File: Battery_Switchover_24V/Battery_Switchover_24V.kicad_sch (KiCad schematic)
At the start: 0 parts

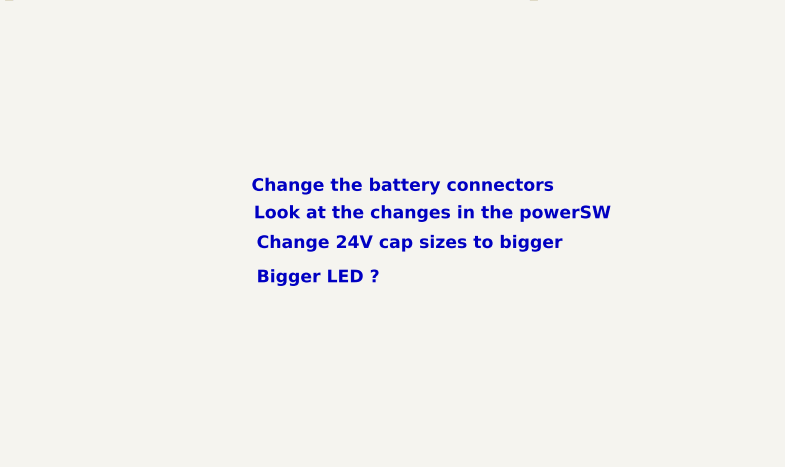
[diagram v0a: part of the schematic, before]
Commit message: Minor placement changes
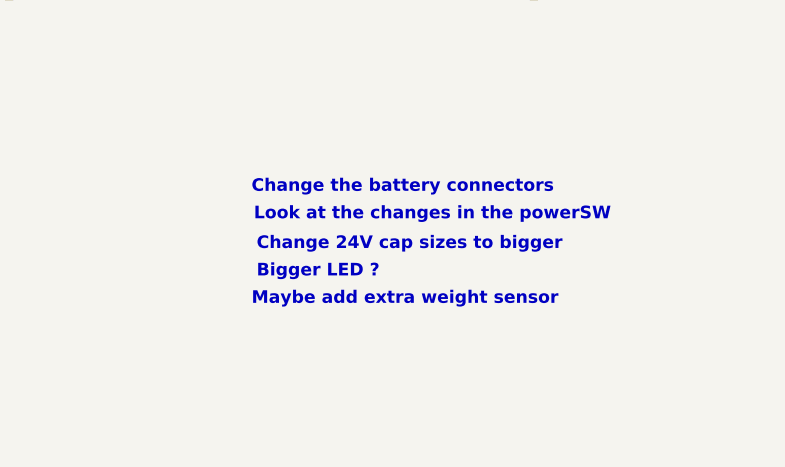
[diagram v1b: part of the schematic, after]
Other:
- note added: "Maybe add extra weight sensor"
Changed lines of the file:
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@@
+		)
+	)
+	(text "Maybe add extra weight sensor"
+		(exclude_from_sim no)
+		(at 201.168 109.22 0)
+		(effects
+			(font
+				(size 1.397 1.397)
+				(thickness 0.2794)
+				(bold yes)
+			)
 		)
 	)
@@
 	(text "Bigger LED ?"
 		(exclude_from_sim no)
-		(at 191.516 106.934 0)
+		(at 191.516 106.172 0)
 		(effects
 			(font

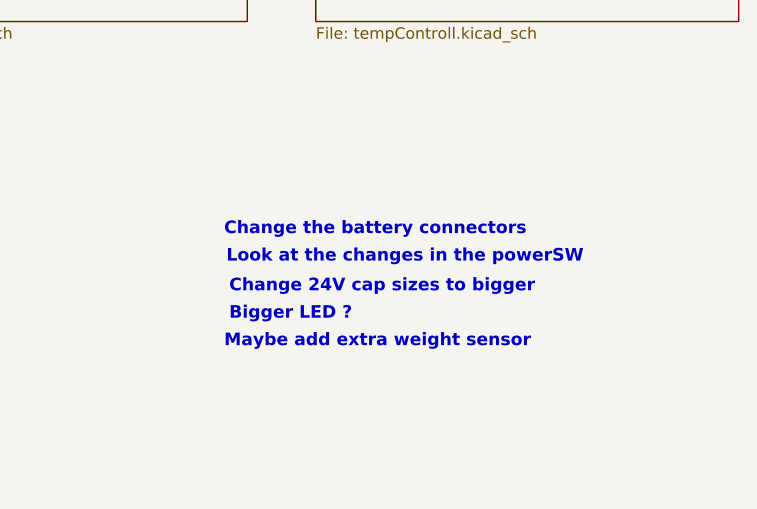
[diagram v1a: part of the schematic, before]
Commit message: Added 6 Pin ATX Connector
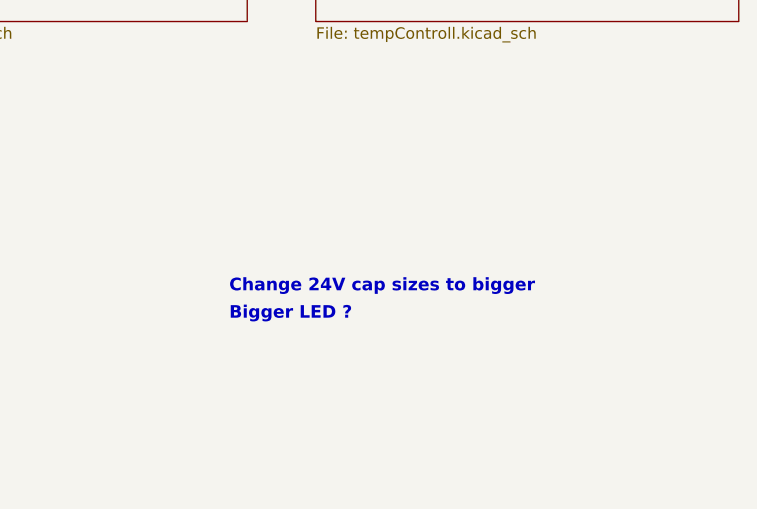
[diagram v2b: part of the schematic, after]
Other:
- note removed: "Change the battery connectors"
- note removed: "Look at the changes in the powerSW"
- note removed: "Maybe add extra weight sensor"
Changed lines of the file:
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@@
-		)
-	)
-	(text "Change the battery connectors"
-		(exclude_from_sim no)
-		(at 200.914 96.774 0)
-		(effects
-			(font
-				(size 1.397 1.397)
-				(thickness 0.2794)
-				(bold yes)
-			)
-		)
-	)
-	(text "Maybe add extra weight sensor"
-		(exclude_from_sim no)
-		(at 201.168 109.22 0)
-		(effects
-			(font
-				(size 1.397 1.397)
-				(thickness 0.2794)
-				(bold yes)
-			)
-		)
-	)
-	(text "Look at the changes in the powerSW"
-		(exclude_from_sim no)
-		(at 204.216 99.822 0)
-		(effects
-			(font
-				(size 1.397 1.397)
-				(thickness 0.254)
-				(bold yes)
-			)
 		)
 	)

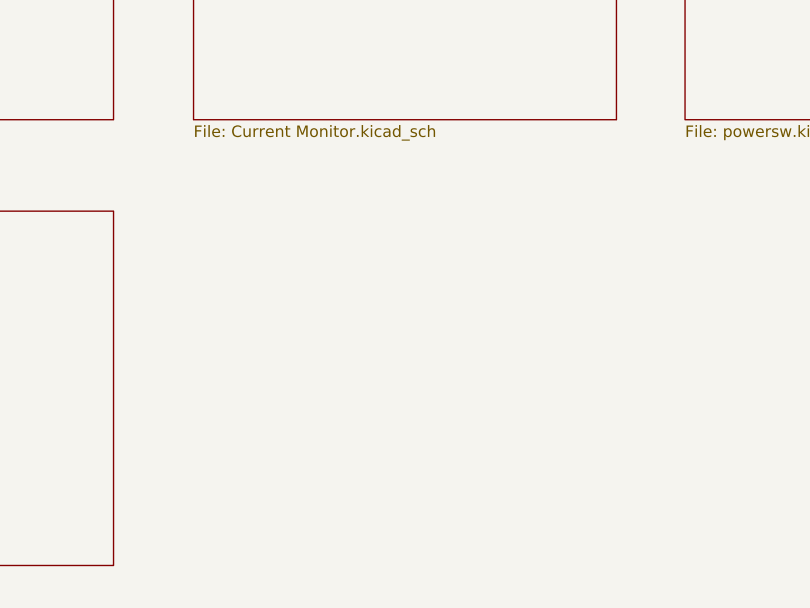
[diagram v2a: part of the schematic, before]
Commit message: added BMS IC
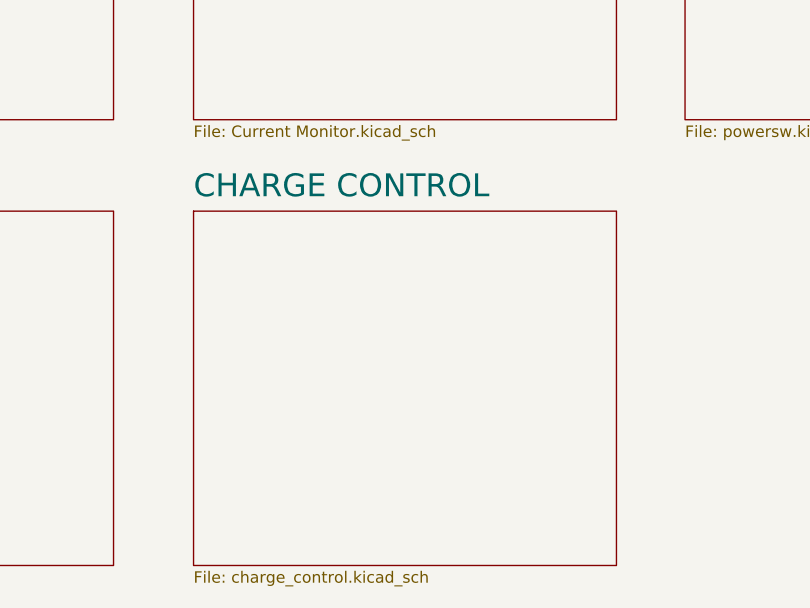
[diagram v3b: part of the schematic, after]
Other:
- added sheet CHARGE CONTROL (charge_control.kicad_sch)
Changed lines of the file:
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@@
+	)
+	(sheet
+		(at 85.09 83.82)
+		(size 46.99 39.37)
+		(exclude_from_sim no)
+		(in_bom yes)
+		(on_board yes)
+		(dnp no)
+		(fields_autoplaced yes)
+		(stroke
+			(width 0.1524)
+			(type solid)
+		)
+		(fill
+			(color 0 0 0 0.0000)
+		)
+		(property "Sheetname" "CHARGE CONTROL"
+			(at 85.09 82.4734 0)
+			(effects
+				(font
+					(size 2.54 2.54)
+				)
+				(justify left bottom)
+			)
+		)
+		(property "Sheetfile" "charge_control.kicad_sch"
+			(at 85.09 123.7746 0)
+			(effects
+				(font
+					(size 1.27 1.27)
+				)
+				(justify left top)
+			)
+		)
+		(instances
+			(project "Battery_Switchover_24V"
+				(path "/045845e0-5d00-4da8-961e-99bdf190f683"
+					(page "7")
+				)
+			)
+		)
 	)
 	(sheet

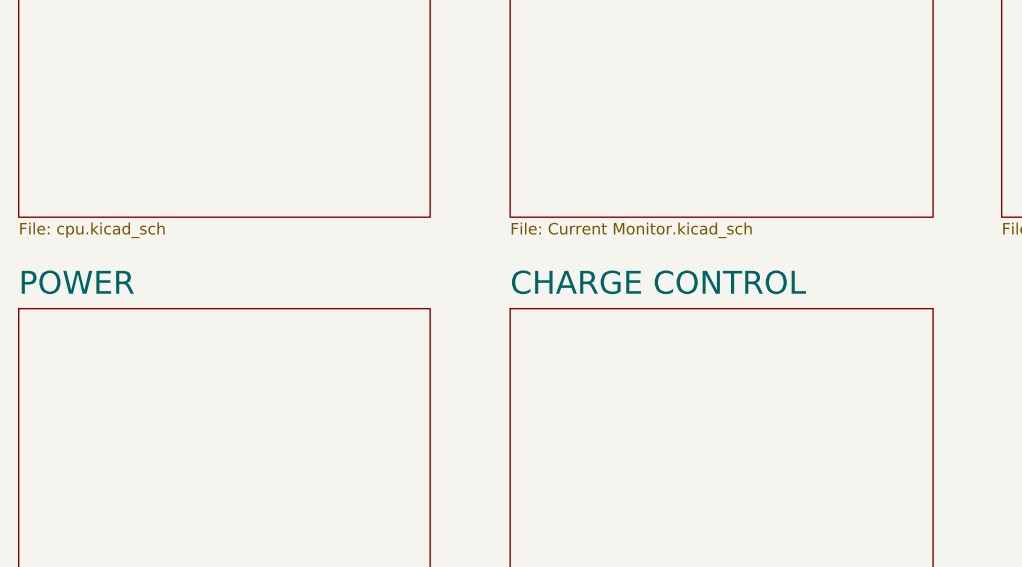
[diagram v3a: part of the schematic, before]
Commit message: aded bms details
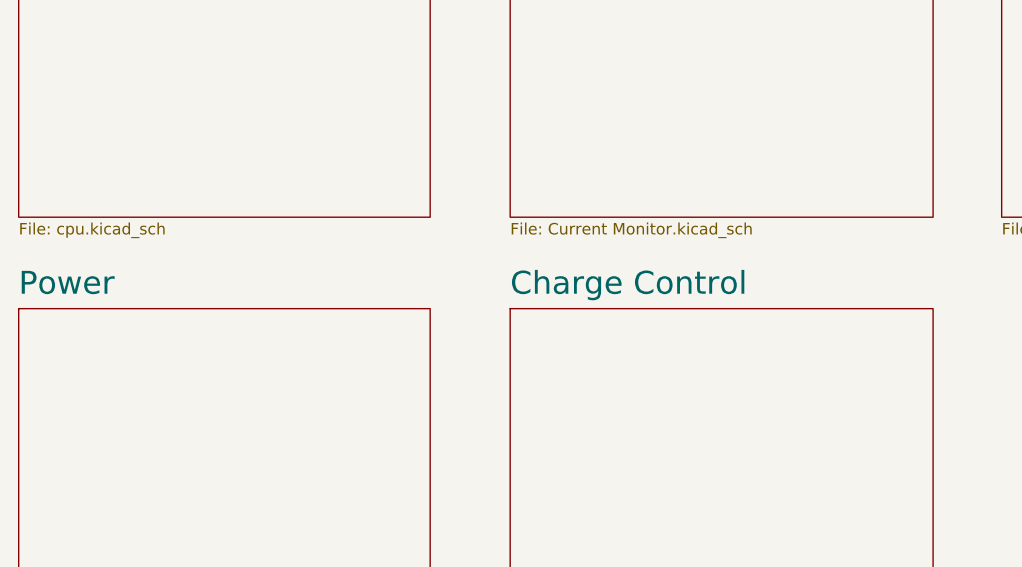
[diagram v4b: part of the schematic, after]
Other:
- sheet CHARGE CONTROL renamed Charge Control
- sheet POWER renamed Power
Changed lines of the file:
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@@
 			(color 0 0 0 0.0000)
 		)
-		(property "Sheetname" "POWER"
+		(property "Sheetname" "Power"
 			(at 30.48 82.4734 0)
 			(effects
@@
 			(color 0 0 0 0.0000)
 		)
-		(property "Sheetname" "CHARGE CONTROL"
+		(property "Sheetname" "Charge Control"
 			(at 85.09 82.4734 0)
 			(effects

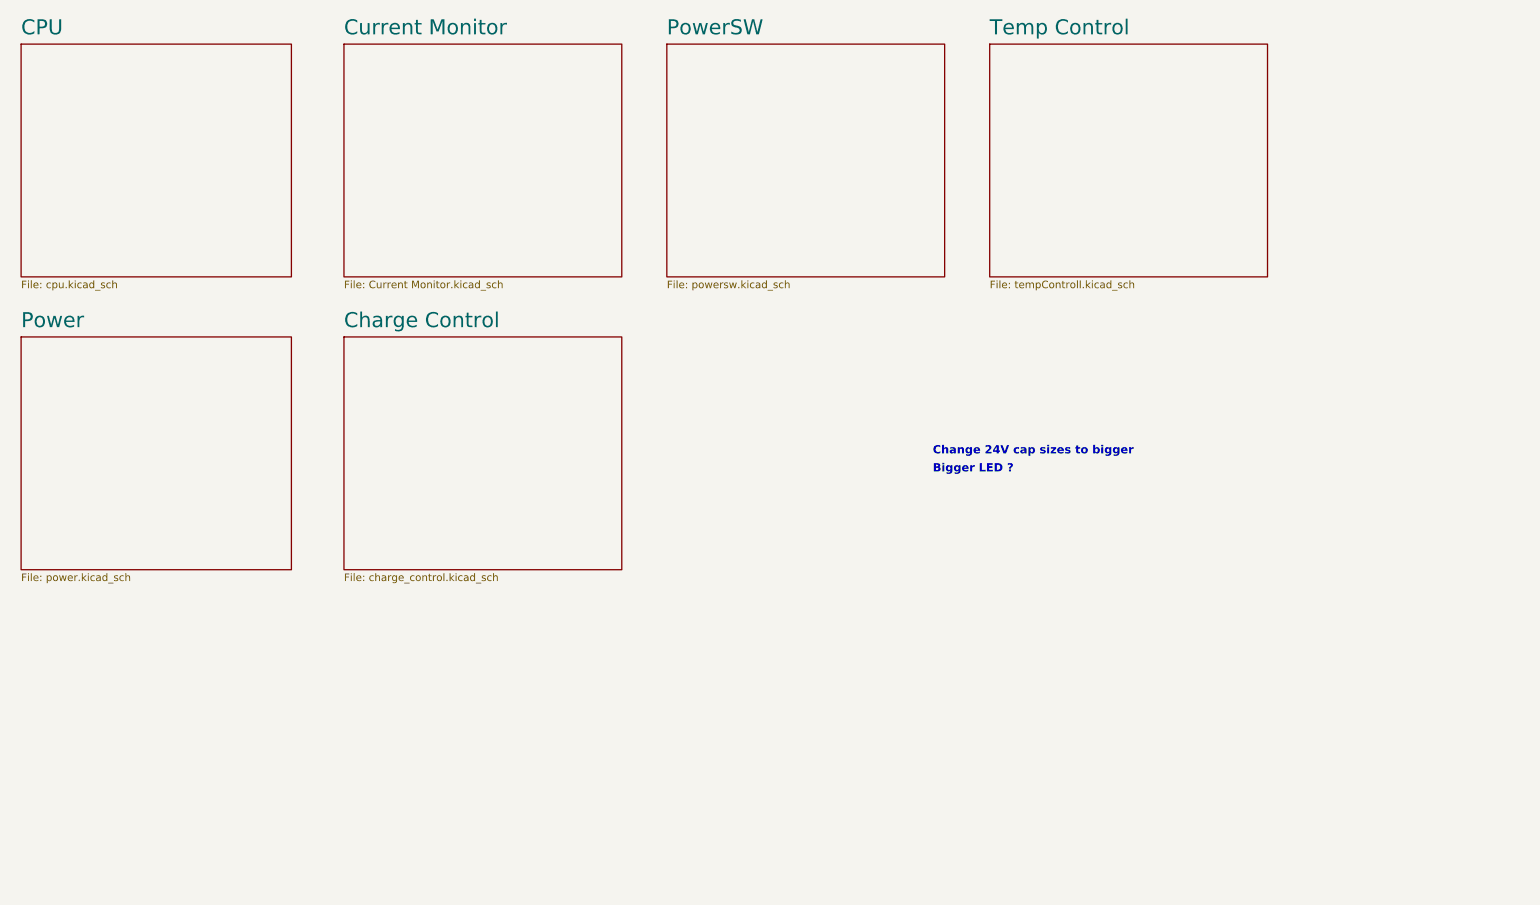
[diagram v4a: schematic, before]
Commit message: adding BMS and changed topology
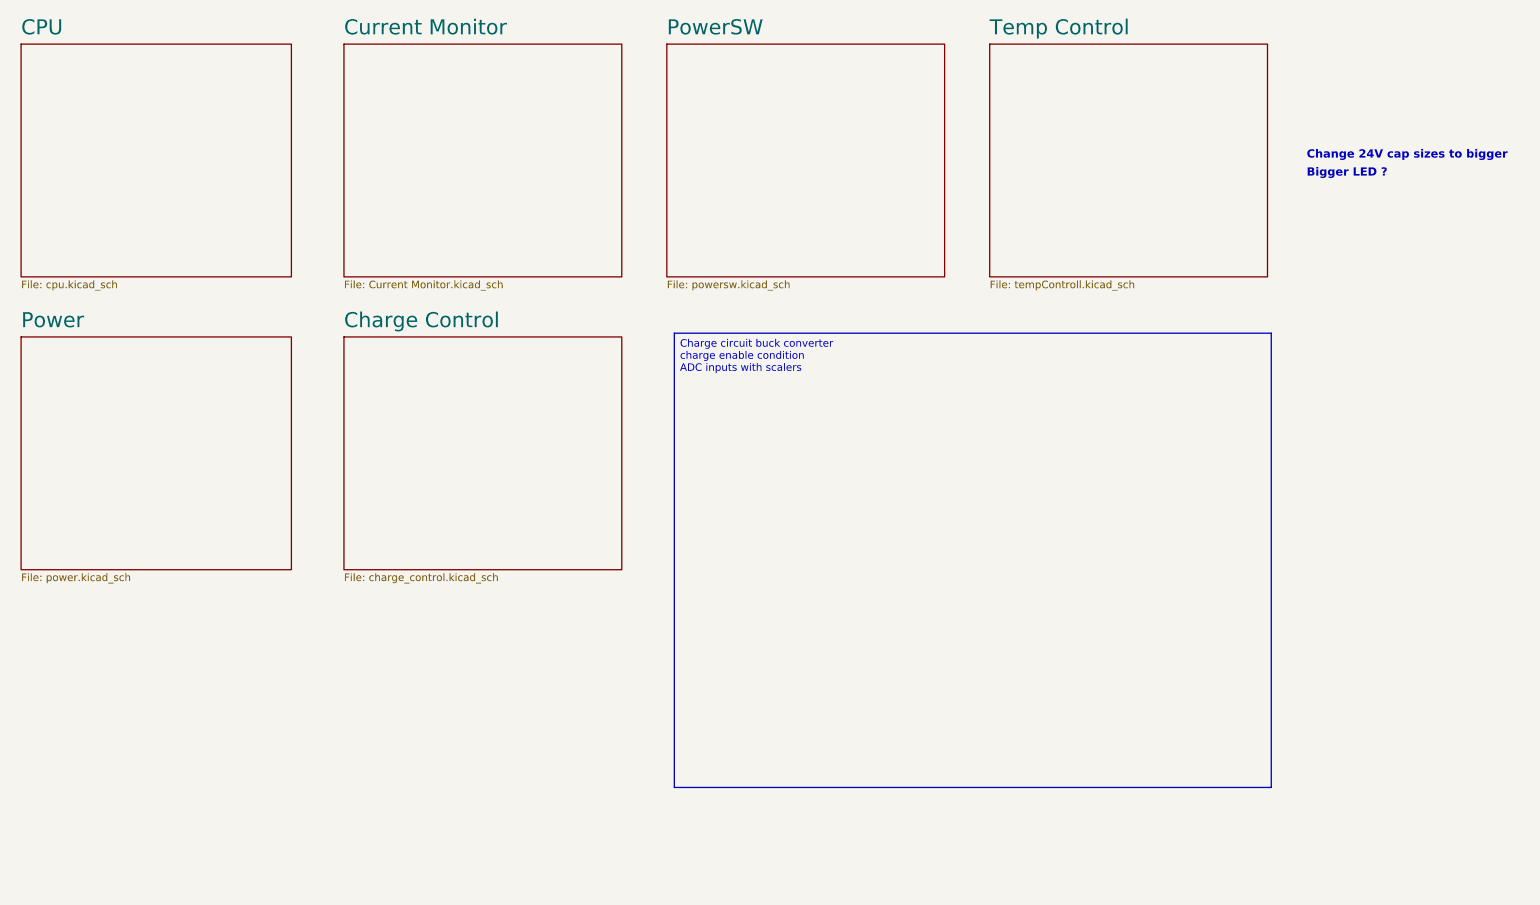
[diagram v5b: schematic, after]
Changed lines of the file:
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@@
 	(text "Change 24V cap sizes to bigger\n"
 		(exclude_from_sim no)
-		(at 201.676 103.124 0)
+		(at 264.922 53.086 0)
 		(effects
 			(font
@@
 	(text "Bigger LED ?"
 		(exclude_from_sim no)
-		(at 191.516 106.172 0)
+		(at 254.762 56.134 0)
 		(effects
 			(font
@@
 		)
 	)
+	(text_box "Charge circuit buck converter\ncharge enable condition\nADC inputs with scalers"
+		(exclude_from_sim no)
+		(at 140.97 83.185 0)
+		(size 100.965 76.835)
+		(margins 0.9525 0.9525 0.9525 0.9525)
+		(stroke
+			(width 0)
+			(type solid)
+		)
+		(fill
+			(type none)
+		)
+		(effects
+			(font
+				(size 1.27 1.27)
+			)
+			(justify left top)
+		)
+	)

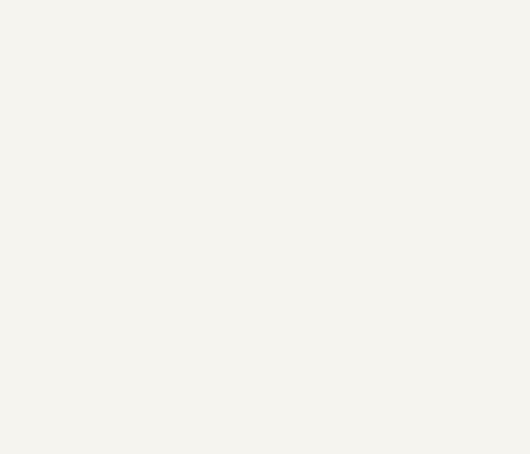
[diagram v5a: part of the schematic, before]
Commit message: adc pins holes
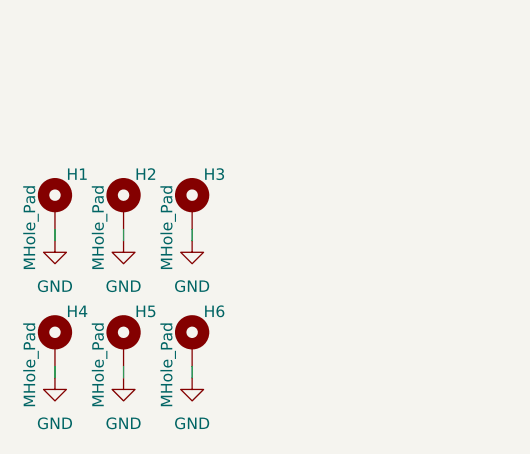
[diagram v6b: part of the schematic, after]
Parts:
- added H1, H2, H3, H4, H5, H6: MHole_Pad, MountingHole:MountingHole_2.5mm_Pad_Via, symbol Mechanical:MountingHole_Pad
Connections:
- new net GND: H1.1, H2.1, H3.1, H4.1, H5.1, H6.1

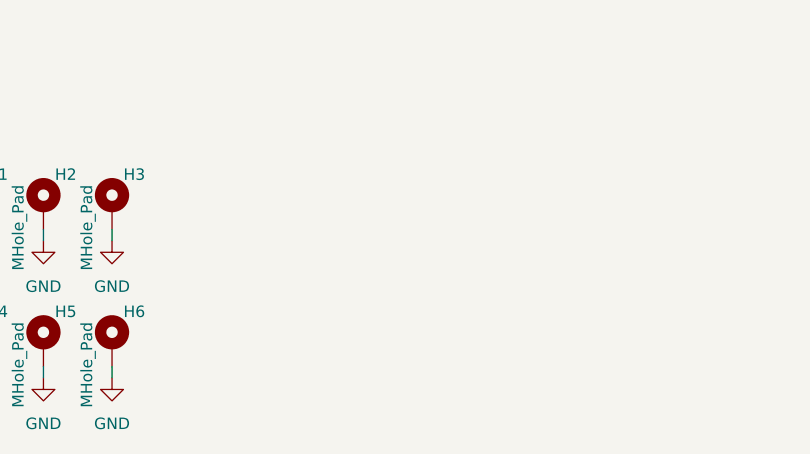
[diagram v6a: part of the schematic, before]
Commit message: Added ATX fuses
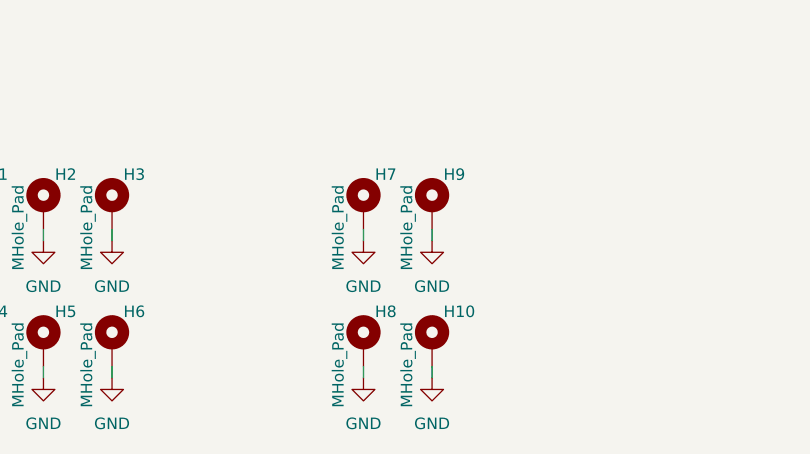
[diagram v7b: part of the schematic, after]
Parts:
- added H10, H7, H8, H9: MHole_Pad, MountingHole:MountingHole_2.5mm_Pad_Via, symbol Mechanical:MountingHole_Pad
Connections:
- net GND: now also H10.1, H7.1, H8.1, H9.1
